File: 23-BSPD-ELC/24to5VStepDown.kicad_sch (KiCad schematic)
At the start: 5 parts

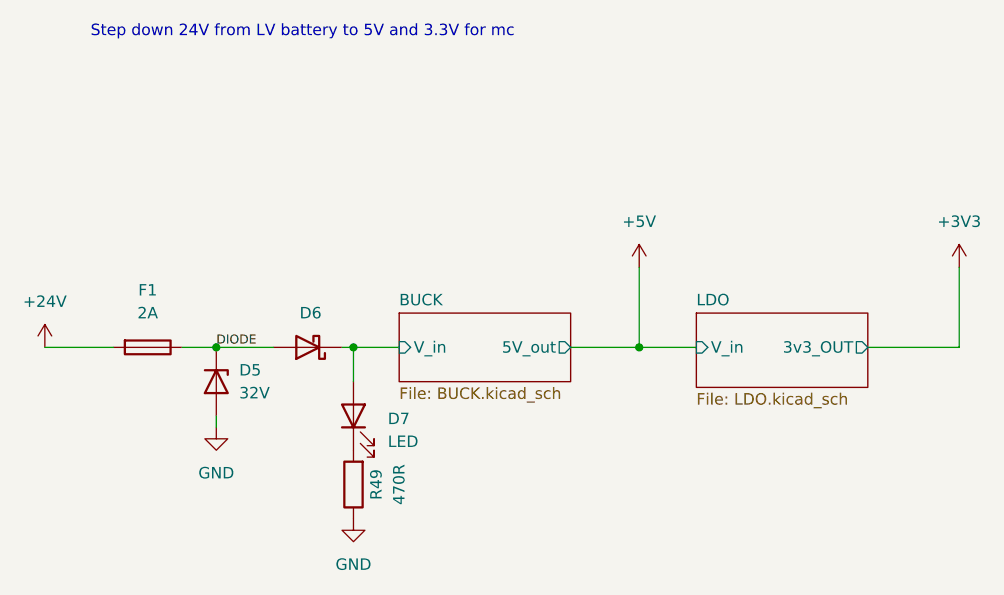
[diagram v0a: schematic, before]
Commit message: Revision changes and updates to some footprints
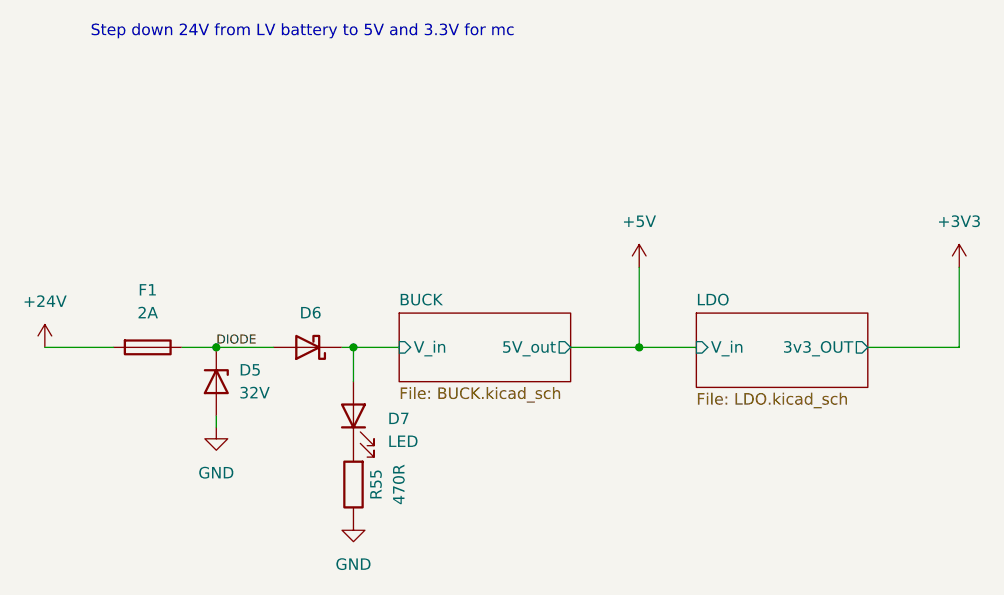
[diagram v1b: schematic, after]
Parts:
- renumbered R49 to R55
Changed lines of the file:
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@@
   (symbol (lib_id "power:+3V3") (at 194.31 81.28 0) (unit 1)
     (in_bom yes) (on_board yes) (fields_autoplaced)
-    (property "Reference" "#PWR0152" (id 0) (at 194.31 85.09 0)
+    (property "Reference" "#PWR0158" (id 0) (at 194.31 85.09 0)
       (effects (font (size 1.27 1.27)) hide)
     )
@@
   (symbol (lib_id "power:+5V") (at 158.75 81.28 0) (unit 1)
     (in_bom yes) (on_board yes) (fields_autoplaced)
-    (property "Reference" "#PWR0151" (id 0) (at 158.75 85.09 0)
+    (property "Reference" "#PWR0157" (id 0) (at 158.75 85.09 0)
       (effects (font (size 1.27 1.27)) hide)
     )
@@
   (symbol (lib_id "power:GND") (at 111.76 99.06 0) (unit 1)
     (in_bom yes) (on_board yes) (fields_autoplaced)
-    (property "Reference" "#PWR0149" (id 0) (at 111.76 105.41 0)
+    (property "Reference" "#PWR0155" (id 0) (at 111.76 105.41 0)
       (effects (font (size 1.27 1.27)) hide)
     )
@@
   (symbol (lib_id "power:+24V") (at 92.71 90.17 0) (unit 1)
     (in_bom yes) (on_board yes) (fields_autoplaced)
-    (property "Reference" "#PWR0148" (id 0) (at 92.71 93.98 0)
+    (property "Reference" "#PWR0154" (id 0) (at 92.71 93.98 0)
       (effects (font (size 1.27 1.27)) hide)
     )
@@
   (symbol (lib_id "Device:R") (at 127 105.41 180) (unit 1)
     (in_bom yes) (on_board yes)
-    (property "Reference" "R49" (id 0) (at 129.54 105.41 90))
+    (property "Reference" "R55" (id 0) (at 129.54 105.41 90))
     (property "Value" "470R" (id 1) (at 132.08 105.41 90))
     (property "Footprint" "Resistor_SMD:R_0603_1608Metric_Pad0.98x0.95mm_HandSolder" (id 2) (at 128.778 105.41 90)
@@
   (symbol (lib_id "power:GND") (at 127 109.22 0) (unit 1)
     (in_bom yes) (on_board yes) (fields_autoplaced)
-    (property "Reference" "#PWR0150" (id 0) (at 127 115.57 0)
+    (property "Reference" "#PWR0156" (id 0) (at 127 115.57 0)
       (effects (font (size 1.27 1.27)) hide)
     )

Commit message: Updated pcb layout; Watchdog on board still in progress
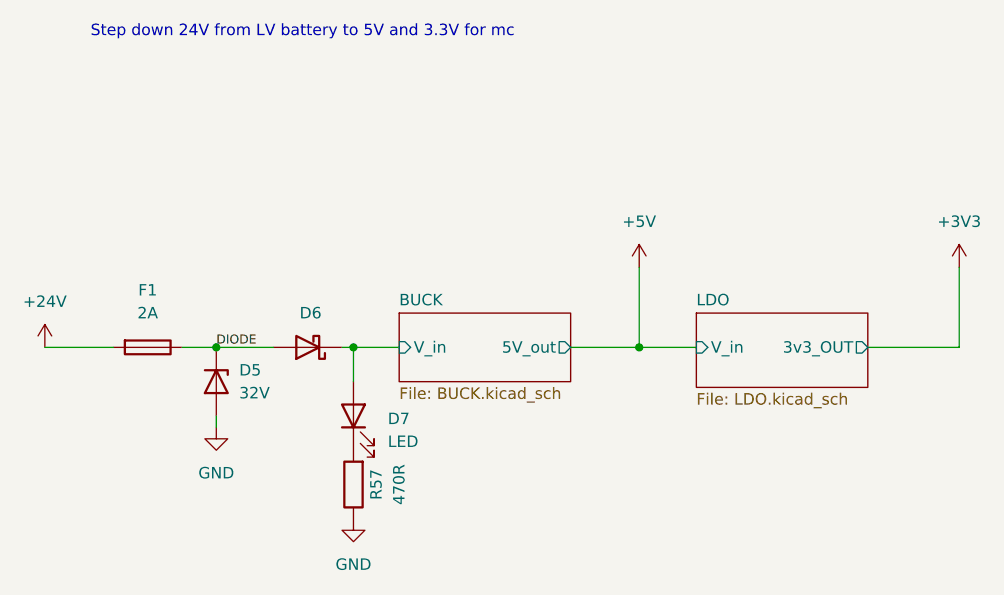
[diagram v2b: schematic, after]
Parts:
- renumbered R55 to R57
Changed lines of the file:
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@@
   (symbol (lib_id "Device:R") (at 127 105.41 180) (unit 1)
     (in_bom yes) (on_board yes)
-    (property "Reference" "R55" (id 0) (at 129.54 105.41 90))
+    (property "Reference" "R57" (id 0) (at 129.54 105.41 90))
     (property "Value" "470R" (id 1) (at 132.08 105.41 90))
     (property "Footprint" "Resistor_SMD:R_0603_1608Metric_Pad0.98x0.95mm_HandSolder" (id 2) (at 128.778 105.41 90)

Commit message: BSPD layout
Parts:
- renumbered R57 to R52
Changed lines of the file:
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@@
   (symbol (lib_id "power:+3V3") (at 194.31 81.28 0) (unit 1)
     (in_bom yes) (on_board yes) (fields_autoplaced)
-    (property "Reference" "#PWR0158" (id 0) (at 194.31 85.09 0)
+    (property "Reference" "#PWR0153" (id 0) (at 194.31 85.09 0)
       (effects (font (size 1.27 1.27)) hide)
     )
@@
   (symbol (lib_id "power:+5V") (at 158.75 81.28 0) (unit 1)
     (in_bom yes) (on_board yes) (fields_autoplaced)
-    (property "Reference" "#PWR0157" (id 0) (at 158.75 85.09 0)
+    (property "Reference" "#PWR0152" (id 0) (at 158.75 85.09 0)
       (effects (font (size 1.27 1.27)) hide)
     )
@@
   (symbol (lib_id "power:GND") (at 111.76 99.06 0) (unit 1)
     (in_bom yes) (on_board yes) (fields_autoplaced)
-    (property "Reference" "#PWR0155" (id 0) (at 111.76 105.41 0)
+    (property "Reference" "#PWR0150" (id 0) (at 111.76 105.41 0)
       (effects (font (size 1.27 1.27)) hide)
     )
@@
   (symbol (lib_id "power:+24V") (at 92.71 90.17 0) (unit 1)
     (in_bom yes) (on_board yes) (fields_autoplaced)
-    (property "Reference" "#PWR0154" (id 0) (at 92.71 93.98 0)
+    (property "Reference" "#PWR0149" (id 0) (at 92.71 93.98 0)
       (effects (font (size 1.27 1.27)) hide)
     )
@@
   (symbol (lib_id "Device:R") (at 127 105.41 180) (unit 1)
     (in_bom yes) (on_board yes)
-    (property "Reference" "R57" (id 0) (at 129.54 105.41 90))
+    (property "Reference" "R52" (id 0) (at 129.54 105.41 90))
     (property "Value" "470R" (id 1) (at 132.08 105.41 90))
     (property "Footprint" "Resistor_SMD:R_0603_1608Metric_Pad0.98x0.95mm_HandSolder" (id 2) (at 128.778 105.41 90)
@@
   (symbol (lib_id "power:GND") (at 127 109.22 0) (unit 1)
     (in_bom yes) (on_board yes) (fields_autoplaced)
-    (property "Reference" "#PWR0156" (id 0) (at 127 115.57 0)
+    (property "Reference" "#PWR0151" (id 0) (at 127 115.57 0)
       (effects (font (size 1.27 1.27)) hide)
     )
